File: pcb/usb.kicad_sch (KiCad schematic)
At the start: 7 parts, among them J4 USB_C_Receptacle_USB2.0_16P, U3 USBLC6-2SC6

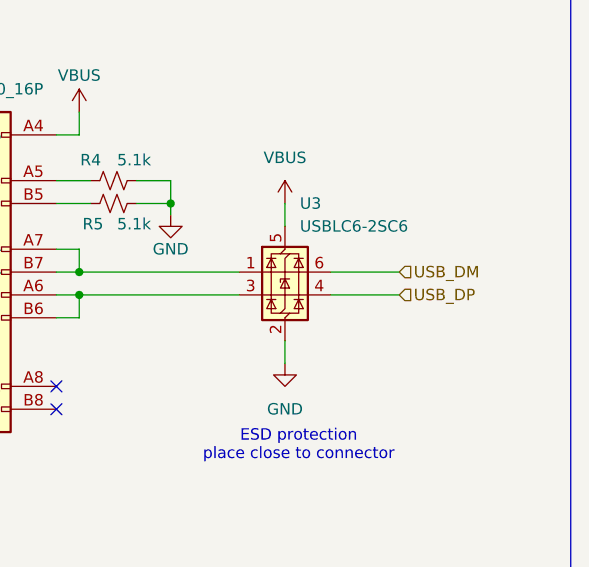
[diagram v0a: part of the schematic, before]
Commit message: Improve inter sheet connections
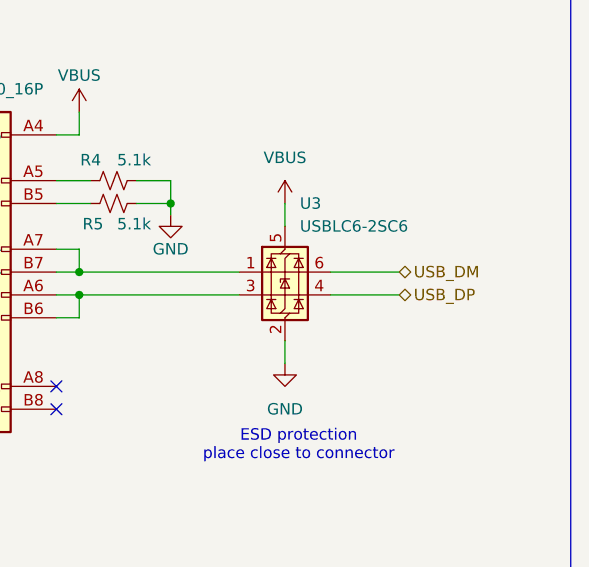
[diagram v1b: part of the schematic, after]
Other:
- title: (none) -> Flight Computer
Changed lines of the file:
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@@
 	(generator_version "9.0")
 	(paper "A4")
+	(title_block
+		(title "Flight Computer")
+	)
 	(rectangle
 		(start 19.05 19.05)
@@
 	)
 	(hierarchical_label "USB_DM"
-		(shape input)
+		(shape bidirectional)
 		(at 88.9 106.68 0)
 		(effects
@@
 	)
 	(hierarchical_label "USB_DP"
-		(shape input)
+		(shape bidirectional)
 		(at 88.9 109.22 0)
 		(effects

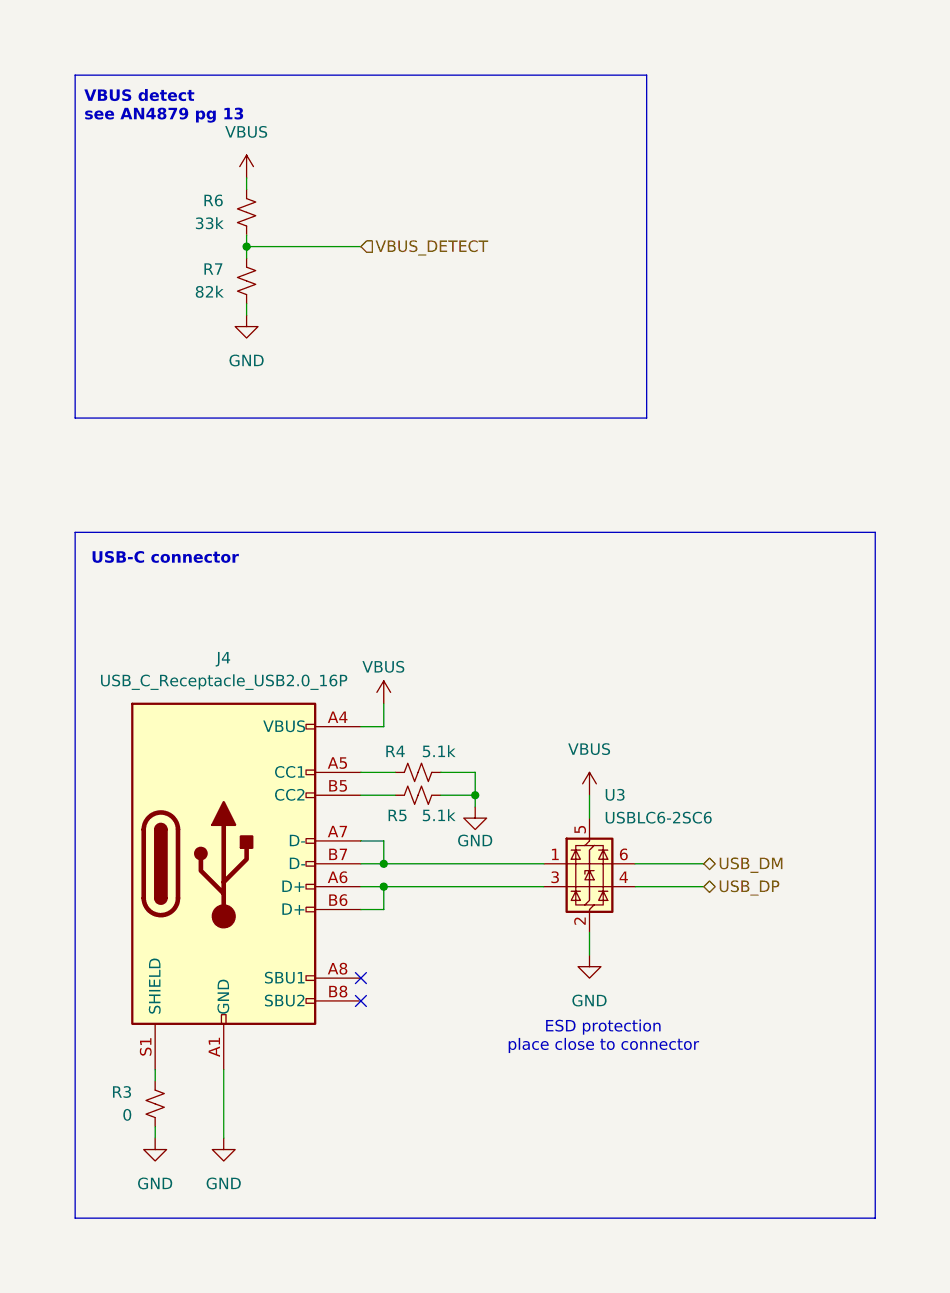
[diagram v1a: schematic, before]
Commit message: Fix pin directionality
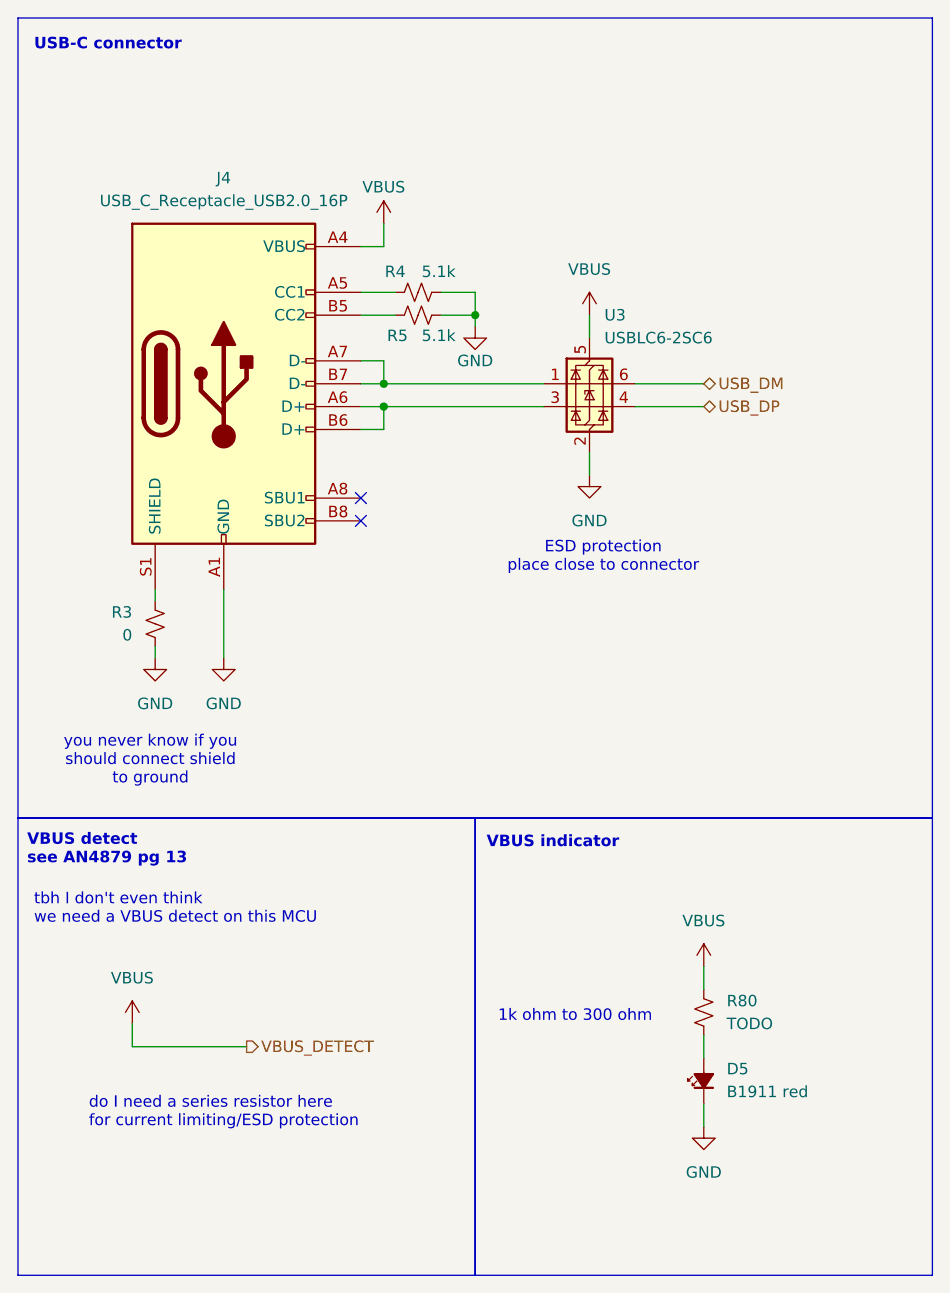
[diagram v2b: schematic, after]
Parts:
- removed R6: 33k, symbol Device:R_Small_US
- removed R7: 82k, symbol Device:R_Small_US
- added D5: B1911 red, symbol Device:LED_Small_Filled
- added R80: TODO, symbol Device:R_Small_US
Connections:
- net GND: now also D5.1 (K)
- net VBUS: now also R80.1
- new net: D5.2 (A), R80.2
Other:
- note added: "1k ohm to 300 ohm"
- note added: "VBUS indicator"
- note added: "do I need a series resistor here for current limiting/ESD protection"
- note added: "tbh I don't even think we need a VBUS detect on this MCU"
- note added: "you never know if you should connect shield to ground"
- moved on the sheet: J4, R3, R4, R5, U3

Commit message: Assign most footprints
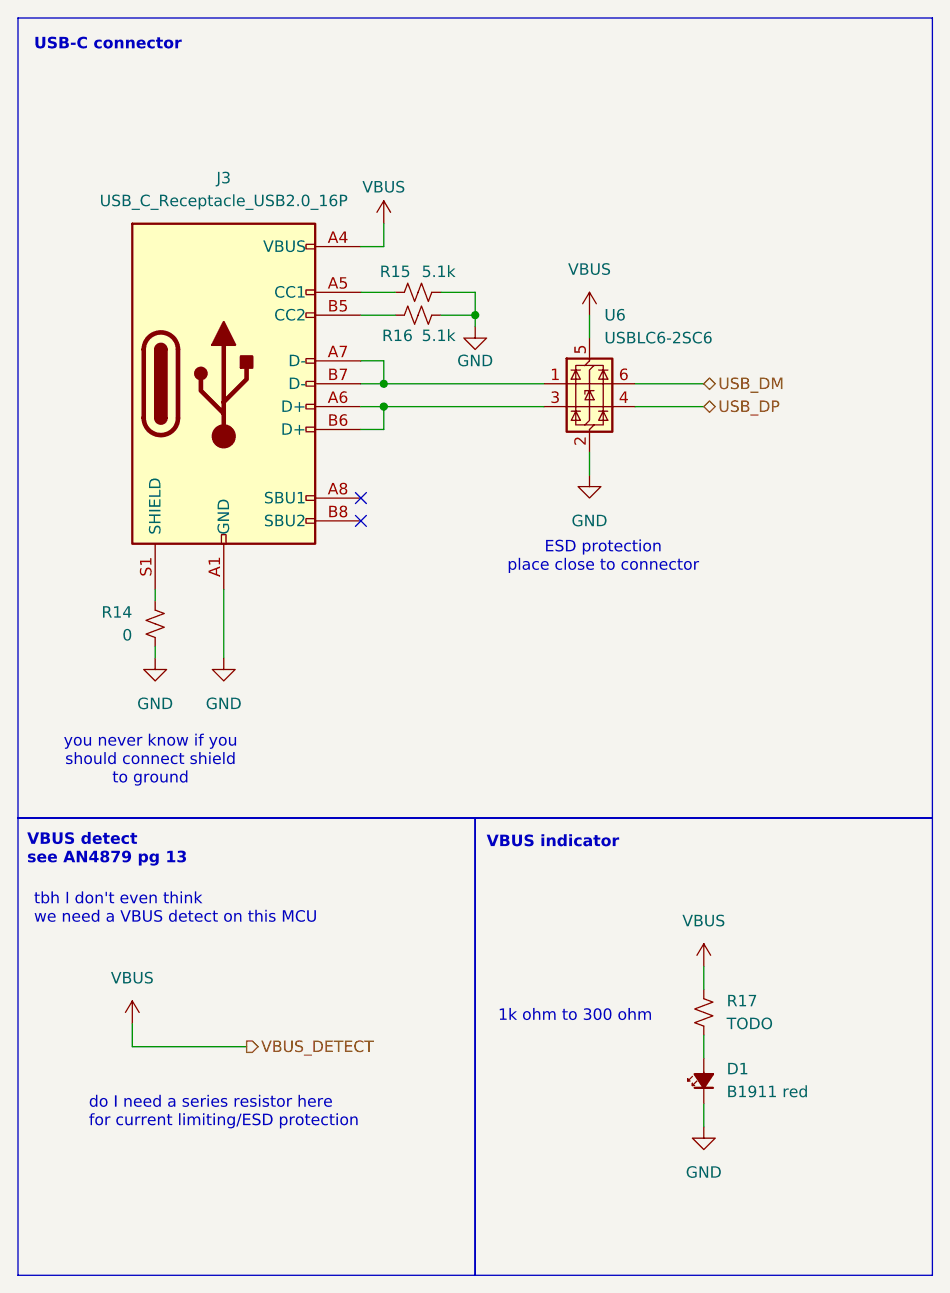
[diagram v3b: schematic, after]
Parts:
- D1: renamed from D5; footprint (none) -> LED_SMD:LED_0603_1608Metric
- R14: renamed from R3; footprint (none) -> Resistor_SMD:R_0603_1608Metric
- R15: renamed from R4; footprint (none) -> Resistor_SMD:R_0603_1608Metric
- R16: renamed from R5; footprint (none) -> Resistor_SMD:R_0603_1608Metric
- R17: renamed from R80; footprint (none) -> Resistor_SMD:R_0603_1608Metric
- renumbered J4 to J3, U3 to U6
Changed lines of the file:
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@@
 		(dnp no)
 		(fields_autoplaced yes)
-		(property "Reference" "R80"
+		(property "Reference" "R17"
 			(at 91.44 121.9199 0)
 			(effects
@@
 			)
 		)
-		(property "Footprint" ""
+		(property "Footprint" "Resistor_SMD:R_0603_1608Metric"
 			(at 88.9 123.19 0)
 			(effects
@@
 			(project ""
 				(path "/84bf90ca-3018-4167-b21c-becfa336d24d/a3f4e773-47f1-4711-b0e8-2c3bb838ada1"
-					(reference "R80")
+					(reference "R17")
 					(unit 1)
 				)
@@
 		(on_board yes)
 		(dnp no)
-		(property "Reference" "R3"
+		(property "Reference" "R14"
 			(at 25.4 78.7399 0)
 			(effects
@@
 			)
 		)
-		(property "Footprint" ""
+		(property "Footprint" "Resistor_SMD:R_0603_1608Metric"
 			(at 27.94 80.01 0)
 			(effects
@@
 			(project ""
 				(path "/84bf90ca-3018-4167-b21c-becfa336d24d/a3f4e773-47f1-4711-b0e8-2c3bb838ada1"
-					(reference "R3")
+					(reference "R14")
 					(unit 1)
 				)
@@
 		(on_board yes)
 		(dnp no)
-		(property "Reference" "R4"
+		(property "Reference" "R15"
 			(at 54.61 40.894 90)
 			(effects
@@
 			)
 		)
-		(property "Footprint" ""
+		(property "Footprint" "Resistor_SMD:R_0603_1608Metric"
 			(at 57.15 43.18 0)
 			(effects
@@
 			(project ""
 				(path "/84bf90ca-3018-4167-b21c-becfa336d24d/a3f4e773-47f1-4711-b0e8-2c3bb838ada1"
-					(reference "R4")
+					(reference "R15")
 					(unit 1)
 				)
@@
 		(dnp no)
 		(fields_autoplaced yes)
-		(property "Reference" "#PWR0114"
+		(property "Reference" "#PWR059"
 			(at 88.9 142.24 0)
 			(effects
@@
 			(project ""
 				(path "/84bf90ca-3018-4167-b21c-becfa336d24d/a3f4e773-47f1-4711-b0e8-2c3bb838ada1"
-					(reference "#PWR0114")
+					(reference "#PWR059")
 					(unit 1)
 				)
@@
 		(dnp no)
 		(fields_autoplaced yes)
-		(property "Reference" "D5"
+		(property "Reference" "D1"
 			(at 91.44 129.4764 90)
 			(effects
@@
 			)
 		)
-		(property "Footprint" ""
+		(property "Footprint" "LED_SMD:LED_0603_1608Metric"
 			(at 88.9 130.81 90)
 			(effects
@@
 			(project ""
 				(path "/84bf90ca-3018-4167-b21c-becfa336d24d/a3f4e773-47f1-4711-b0e8-2c3bb838ada1"
-					(reference "D5")
+					(reference "D1")
 					(unit 1)
 				)
@@
 		(dnp no)
 		(fields_autoplaced yes)
-		(property "Reference" "J4"
+		(property "Reference" "J3"
 			(at 35.56 30.48 0)
 			(effects
@@
 			(project ""
 				(path "/84bf90ca-3018-4167-b21c-becfa336d24d/a3f4e773-47f1-4711-b0e8-2c3bb838ada1"
-					(reference "J4")
+					(reference "J3")
 					(unit 1)
 				)
@@
 		(dnp no)
 		(fields_autoplaced yes)
-		(property "Reference" "#PWR031"
+		(property "Reference" "#PWR051"
 			(at 25.4 128.27 0)
 			(effects
@@
 			(project "flight-computer"
 				(path "/84bf90ca-3018-4167-b21c-becfa336d24d/a3f4e773-47f1-4711-b0e8-2c3bb838ada1"
-					(reference "#PWR031")
+					(reference "#PWR051")
 					(unit 1)
 				)
@@
 		(on_board yes)
 		(dnp no)
-		(property "Reference" "#PWR027"
+		(property "Reference" "#PWR055"
 			(at 63.5 53.34 0)
 			(effects
@@
 			(project ""
 				(path "/84bf90ca-3018-4167-b21c-becfa336d24d/a3f4e773-47f1-4711-b0e8-2c3bb838ada1"
-					(reference "#PWR027")
+					(reference "#PWR055")
 					(unit 1)
 				)
@@
 		(dnp no)
 		(fields_autoplaced yes)
-		(property "Reference" "#PWR029"
+		(property "Reference" "#PWR056"
 			(at 76.2 49.53 0)
 			(effects
@@
 			(project "flight-computer"
 				(path "/84bf90ca-3018-4167-b21c-becfa336d24d/a3f4e773-47f1-4711-b0e8-2c3bb838ada1"
-					(reference "#PWR029")
+					(reference "#PWR056")
 					(unit 1)
 				)
@@
 		(dnp no)
 		(fields_autoplaced yes)
-		(property "Reference" "#PWR026"
+		(property "Reference" "#PWR052"
 			(at 27.94 90.17 0)
 			(effects
@@
 			(project "flight-computer"
 				(path "/84bf90ca-3018-4167-b21c-becfa336d24d/a3f4e773-47f1-4711-b0e8-2c3bb838ada1"
-					(reference "#PWR026")
+					(reference "#PWR052")
 					(unit 1)
 				)
@@
 		(on_board yes)
 		(dnp no)
-		(property "Reference" "R5"
+		(property "Reference" "R16"
 			(at 54.864 48.006 90)
 			(effects
@@
 			)
 		)
-		(property "Footprint" ""
+		(property "Footprint" "Resistor_SMD:R_0603_1608Metric"
 			(at 57.15 45.72 0)
 			(effects
@@
 			(project "flight-computer"
 				(path "/84bf90ca-3018-4167-b21c-becfa336d24d/a3f4e773-47f1-4711-b0e8-2c3bb838ada1"
-					(reference "R5")
+					(reference "R16")
 					(unit 1)
 				)
@@
 		(dnp no)
 		(fields_autoplaced yes)
-		(property "Reference" "U3"
+		(property "Reference" "U6"
 			(at 77.8511 45.72 0)
 			(effects
@@
 			(project ""
 				(path "/84bf90ca-3018-4167-b21c-becfa336d24d/a3f4e773-47f1-4711-b0e8-2c3bb838ada1"
-					(reference "U3")
+					(reference "U6")
 					(unit 1)
 				)
@@
 		(dnp no)
 		(fields_autoplaced yes)
-		(property "Reference" "#PWR0113"
+		(property "Reference" "#PWR058"
 			(at 88.9 121.92 0)
 			(effects
@@
 			(project ""
 				(path "/84bf90ca-3018-4167-b21c-becfa336d24d/a3f4e773-47f1-4711-b0e8-2c3bb838ada1"
-					(reference "#PWR0113")
+					(reference "#PWR058")
 					(unit 1)
 				)
@@
 		(dnp no)
 		(fields_autoplaced yes)
-		(property "Reference" "#PWR030"
+		(property "Reference" "#PWR057"
 			(at 76.2 69.85 0)
 			(effects
@@
 			(project "flight-computer"
 				(path "/84bf90ca-3018-4167-b21c-becfa336d24d/a3f4e773-47f1-4711-b0e8-2c3bb838ada1"
-					(reference "#PWR030")
+					(reference "#PWR057")
 					(unit 1)
 				)
@@
 		(on_board yes)
 		(dnp no)
-		(property "Reference" "#PWR028"
+		(property "Reference" "#PWR054"
 			(at 53.34 39.37 0)
 			(effects
@@
 			(project ""
 				(path "/84bf90ca-3018-4167-b21c-becfa336d24d/a3f4e773-47f1-4711-b0e8-2c3bb838ada1"
-					(reference "#PWR028")
+					(reference "#PWR054")
 					(unit 1)
 				)
@@
 		(dnp no)
 		(fields_autoplaced yes)
-		(property "Reference" "#PWR025"
+		(property "Reference" "#PWR053"
 			(at 35.56 90.17 0)
 			(effects
@@
 			(project ""
 				(path "/84bf90ca-3018-4167-b21c-becfa336d24d/a3f4e773-47f1-4711-b0e8-2c3bb838ada1"
-					(reference "#PWR025")
-					(unit 1)
-				)
+					(reference "#PWR053")
+					(unit 1)
+				)

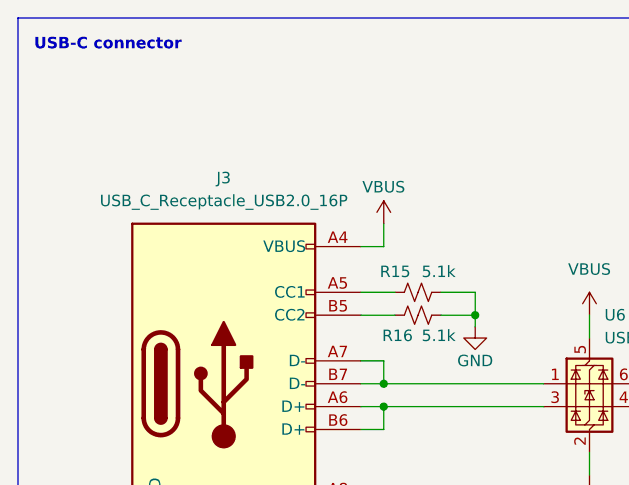
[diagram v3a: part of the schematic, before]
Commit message: Update footprints
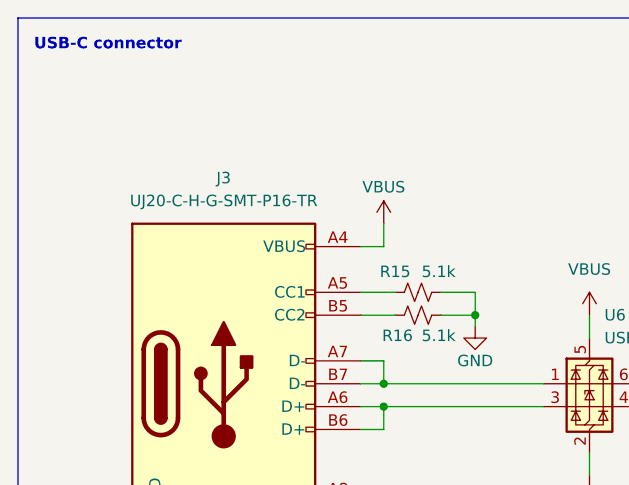
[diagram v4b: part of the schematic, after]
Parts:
- J3: value USB_C_Receptacle_USB2.0_16P -> UJ20-C-H-G-SMT-P16-TR; footprint (none) -> SAMESKY_UJ20-C-H-G-SMT-P16-TR:SAMESKY_UJ20-C-H-G-SMT-P16-TR
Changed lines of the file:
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@@
 			)
 		)
-		(property "Value" "USB_C_Receptacle_USB2.0_16P"
+		(property "Value" "UJ20-C-H-G-SMT-P16-TR"
 			(at 35.56 33.02 0)
 			(effects
@@
 			)
 		)
-		(property "Footprint" ""
+		(property "Footprint" "SAMESKY_UJ20-C-H-G-SMT-P16-TR:SAMESKY_UJ20-C-H-G-SMT-P16-TR"
 			(at 39.37 53.34 0)
 			(effects
